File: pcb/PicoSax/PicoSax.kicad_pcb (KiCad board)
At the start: 2 copper layers, 100 x 160 mm, 80 parts, among them J3 Conn_01x02, M1 MountingHole_3.2mm_M3, M2 MountingHole_3.2mm_M3, M3 MountingHole_3.2mm_M3, M4 MountingHole_3.2mm_M3, M5 MountingHole_3.2mm_M3, M6 MountingHole_3.2mm_M3, SW8va1 Omron_B3K_L13L, SW8vb1 Omron_B3K_L13L, U1 Perfboard

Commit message: USB MIDI minor PCB tweaks
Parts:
- added M5: MountingHole_3.2mm_M3, MountingHole:MountingHole_3.2mm_M3, F.Cu at (125.0, 70.0)
- added M5: MountingHole_3.2mm_M3, MountingHole:MountingHole_3.2mm_M3, F.Cu at (75.0, 70.0)
- moved M6 5.00 mm to (140.0, 180.0)
- moved R16 1.00 mm to (137.0, 187.0)
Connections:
- U1 pad : (no net) -> GND
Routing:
- net /Dup: track 134.0 -> 136.9 mm
- net /Bb: track 147.4 -> 150.3 mm
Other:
- outline, holes or cut-outs redrawn

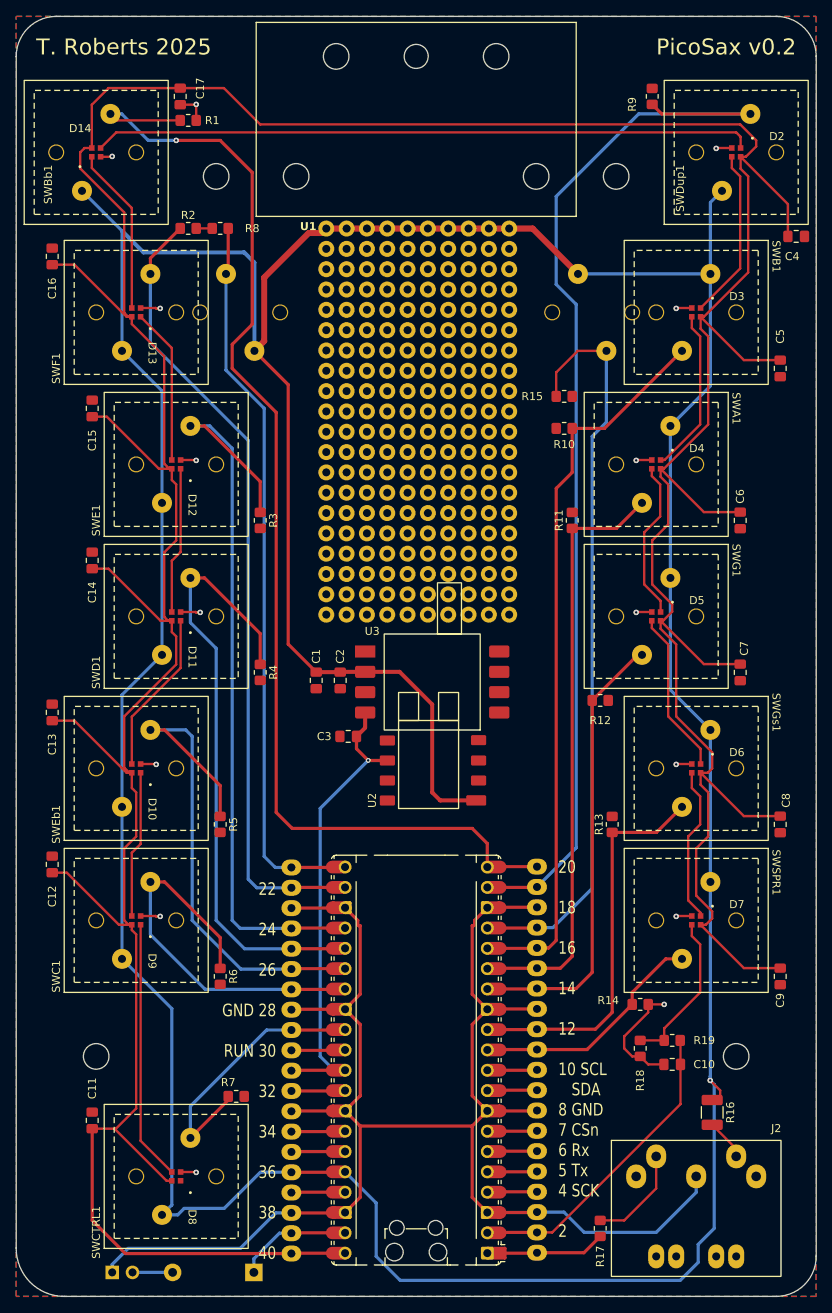
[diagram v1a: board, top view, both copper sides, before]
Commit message: KS-33 Update
Routing still required.  If wanting to work on previous version, see Backup.
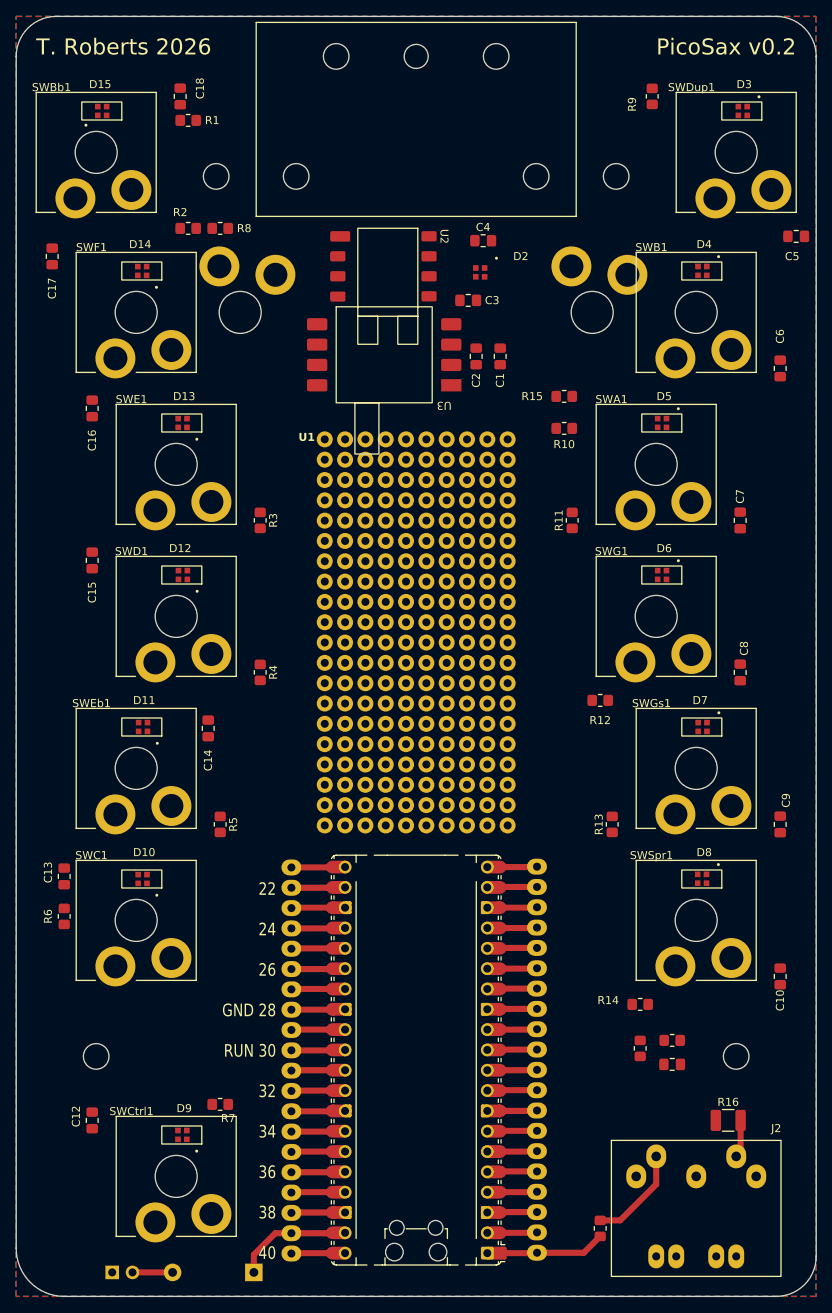
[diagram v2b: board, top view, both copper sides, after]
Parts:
- removed SWCTRL1, SWSPR1: Omron_B3K_L13L, MyLibrary:Omron B3K L13L
- added C4: 0.1uF, Capacitor_SMD:C_0805_2012Metric_Pad1.18x1.45mm_HandSolder, F.Cu at (108.4, 78.0)
- added D2: 19-C47/RSGHBHC-5V01/2T, PicoSax:19-C47_RSGHBHC-5V01-2T, F.Cu at (108.0, 82.0)
- added SWCtrl1: Gateron_KS-33, PicoSax:KS-33, F.Cu at (70.0, 195.0)
- added SWSpr1: Gateron_KS-33, PicoSax:KS-33, F.Cu at (135.0, 163.0)
- SW8va1, SW8vb1, SWA1, SWB1, SWBb1, SWC1, SWD1, SWDup1, SWE1, SWEb1, SWF1, SWG1, SWGs1: value Omron_B3K_L13L -> Gateron_KS-33; footprint MyLibrary:Omron B3K L13L -> PicoSax:KS-33
- moved U2 63.0 mm to (90.2, 82.5), turned to -90 degrees
- moved C3 56.5 mm to (106.5, 85.5), turned to 0 degrees
- moved C1 46.6 mm to (110.5, 92.5), turned to -90 degrees
- moved C2 43.9 mm to (107.5, 92.5), turned to -90 degrees
- moved U3 35.0 mm to (104.4, 96.1), turned to 0 degrees
- moved U1 26.4 mm to (88.6, 102.9)
- moved R6 20.9 mm to (56.0, 162.5), turned to 90 degrees
- moved C14 19.6 mm to (74.0, 139.0)
- moved D8 5.25 mm to (135.7, 157.8)
- moved D9 5.25 mm to (70.8, 189.8)
- moved D4 5.25 mm to (135.8, 81.8)
- moved D10 5.24 mm to (65.8, 157.8)
- moved D13 5.24 mm to (70.8, 100.8)
- moved D11 5.24 mm to (65.9, 138.8)
- moved D12 5.24 mm to (70.8, 119.8)
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- renumbered C9 to C10, C10 to C11, C11 to C12, C12 to C13, C13 to C14, C14 to C15, C15 to C16, C16 to C17, C17 to C18, C4 to C5, C5 to C6, C6 to C7, C7 to C8, C8 to C9, D9 to D10, D10 to D11, D11 to D12, D12 to D13, D13 to D14, D14 to D15, D2 to D3, D3 to D4, D4 to D5, D5 to D6, D6 to D7, D7 to D8, D8 to D9
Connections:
- A1 pad 39: Net-(A1-VSYS) -> /VSYS
- C10 pad 1: +5V -> /VSYS
- C12 pad 1: +5V -> /VSYS
- C13 pad 1: +5V -> /VSYS
- C14 pad 1: +5V -> /VSYS
- C15 pad 1: +5V -> /VSYS
- C16 pad 1: +5V -> /VSYS
- C17 pad 1: +5V -> /VSYS
- C18 pad 1: +5V -> /VSYS
- C5 pad 1: +5V -> /VSYS
- C6 pad 1: +5V -> /VSYS
- C7 pad 1: +5V -> /VSYS
- C8 pad 1: +5V -> /VSYS
- C9 pad 1: +5V -> /VSYS
- D1 pad 1: Net-(A1-VSYS) -> /VSYS
- D10 pad 2: +5V -> /VSYS
- D11 pad 2: +5V -> /VSYS
- D12 pad 2: +5V -> /VSYS
- D13 pad 2: +5V -> /VSYS
- D14 pad 2: +5V -> /VSYS
- D15 pad 2: +5V -> /VSYS
- D15 pad 3: Net-(D14-DIn) (its old number) -> Net-(D15-DIn)
- D3 pad 1: Net-(D14-DIn) (its old number) -> Net-(D2-DIn)
- D3 pad 2: +5V -> /VSYS
- D4 pad 2: +5V -> /VSYS
- D5 pad 2: +5V -> /VSYS
- D6 pad 2: +5V -> /VSYS
- D7 pad 2: +5V -> /VSYS
- D8 pad 2: +5V -> /VSYS
- D9 pad 2: +5V -> /VSYS
- J4 pad 19: Net-(A1-VSYS) -> /VSYS
- U1 pad : GND -> (no net)
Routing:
- net +5V: track 538.0 -> 6.73 mm
- net +3V3: track 534.8 -> 6.73 mm, vias 1 -> 0
- net GND: track 250.0 -> 51.8 mm, vias 15 -> 0
- net /Bb: track 150.3 -> 6.23 mm, vias 1 -> 0
- net /Dup: track 136.9 -> 6.23 mm
- net /F: track 100.5 -> 6.73 mm
- net /E: track 95.4 -> 6.73 mm
- net /8va: track 93.5 -> 6.23 mm
- net /B: track 91.6 -> 6.23 mm
- net /8vb: track 91.3 -> 6.73 mm
- net Net-(D14-DIn) (its old number): track 82.4 -> 0.00 mm
- net /D: track 77.2 -> 6.73 mm
- net /A: track 74.8 -> 6.23 mm
- net /Eb: track 65.7 -> 6.73 mm
- net Net-(A1-GPIO26_ADC0): track 59.6 -> 6.73 mm, vias 1 -> 0
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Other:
- board text added: "T. Roberts 2026"
- board text removed: "20 18 16 14 12 10 SCL SDA 8 GND 7 CSn 6 Rx 5 Tx 4 SCK 2"
- board text removed: "T. Roberts 2025"

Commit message: Partial Route
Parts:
- added R20: 0, Resistor_SMD:R_0805_2012Metric_Pad1.20x1.40mm_HandSolder, F.Cu at (57.5, 194.0)
- added R21: 0, Resistor_SMD:R_0805_2012Metric_Pad1.20x1.40mm_HandSolder, F.Cu at (57.5, 198.0)
- added R22: 0, Resistor_SMD:R_0805_2012Metric_Pad1.20x1.40mm_HandSolder, F.Cu at (57.5, 190.0)
- D1, J3: moved to F.Cu
- moved R10 27.0 mm to (144.0, 92.5), turned to 90 degrees
- moved C5 23.0 mm to (131.0, 61.5), turned to -90 degrees
- moved R2 22.3 mm to (56.0, 92.5), turned to 90 degrees
- moved R15 20.9 mm to (126.0, 78.0), turned to 180 degrees
- moved R11 19.6 mm to (139.0, 111.5)
- moved R13 19.6 mm to (144.0, 149.5)
- moved R3 19.6 mm to (61.0, 111.5), turned to 90 degrees
- moved R4 19.6 mm to (61.0, 130.5), turned to 90 degrees
- moved R5 19.6 mm to (56.0, 149.5), turned to 90 degrees
- moved C14 19.0 mm to (56.0, 145.0), turned to -90 degrees
- moved R12 16.8 mm to (139.0, 130.5), turned to 90 degrees
- moved R14 16.8 mm to (144.0, 168.5), turned to 90 degrees
- moved R9 12.6 mm to (131.0, 72.5)
- moved R1 9.82 mm to (69.0, 72.5), turned to 90 degrees
- moved C15 8.14 mm to (61.0, 126.0), turned to -90 degrees
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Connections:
- C10 pad 1: /VSYS -> /VLED
- C12 pad 1: /VSYS -> /VLED
- C13 pad 1: /VSYS -> /VLED
- C14 pad 1: /VSYS -> /VLED
- C15 pad 1: /VSYS -> /VLED
- C16 pad 1: /VSYS -> /VLED
- C17 pad 1: /VSYS -> /VLED
- C18 pad 1: /VSYS -> /VLED
- C4 pad 1: /VSYS -> /VLED
- C5 pad 1: /VSYS -> /VLED
- C6 pad 1: /VSYS -> /VLED
- C7 pad 1: /VSYS -> /VLED
- C8 pad 1: /VSYS -> /VLED
- C9 pad 1: /VSYS -> /VLED
- D10 pad 2: /VSYS -> /VLED
- D11 pad 2: /VSYS -> /VLED
- D12 pad 2: /VSYS -> /VLED
- D13 pad 2: /VSYS -> /VLED
- D14 pad 2: /VSYS -> /VLED
- D15 pad 2: /VSYS -> /VLED
- D2 pad 2: /VSYS -> /VLED
- D3 pad 2: /VSYS -> /VLED
- D4 pad 2: /VSYS -> /VLED
- D5 pad 2: /VSYS -> /VLED
- D6 pad 2: /VSYS -> /VLED
- D7 pad 2: /VSYS -> /VLED
- D8 pad 2: /VSYS -> /VLED
- D9 pad 2: /VSYS -> /VLED
- SWC1 pad 1: +3V3 -> /C
- SWC1 pad 2: /C -> +3V3
- SWD1 pad 1: +3V3 -> /D
- SWD1 pad 2: /D -> +3V3
- SWDup1 pad 1: +3V3 -> /Dup
- SWDup1 pad 2: /Dup -> +3V3
- SWE1 pad 1: +3V3 -> /E
- SWE1 pad 2: /E -> +3V3
- SWEb1 pad 1: +3V3 -> /Eb
- SWEb1 pad 2: /Eb -> +3V3
- SWF1 pad 1: +3V3 -> /F
- SWF1 pad 2: /F -> +3V3
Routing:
- net /VLED: track 0.00 -> 522.2 mm
- net +3V3: track 6.73 -> 424.1 mm, vias 0 -> 2
- net /Bb: track 6.23 -> 132.2 mm, vias 0 -> 1
- net Net-(A1-GPIO26_ADC0): track 6.73 -> 122.3 mm, vias 0 -> 1
- net /Dup: track 6.23 -> 110.2 mm
- net GND: track 51.8 -> 146.3 mm
- net /B: track 6.23 -> 99.9 mm, vias 0 -> 1
- net /8va: track 6.23 -> 97.9 mm
- net /A: track 6.23 -> 79.6 mm, vias 0 -> 1
- net /G: track 6.23 -> 63.1 mm, vias 0 -> 1
- net Net-(D15-DIn): track 0.00 -> 54.3 mm
- net /Gs: track 6.23 -> 50.9 mm, vias 0 -> 1
- net Net-(D2-DIn): track 0.00 -> 44.4 mm
- net +5V: track 6.73 -> 51.1 mm
- net /Spr: track 6.23 -> 40.6 mm
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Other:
- board text added: "19 17 15 13 11 9 7 5 3 1"
- board text added: "4.5-5.5V"
- board text removed: "1.8-5.5V"

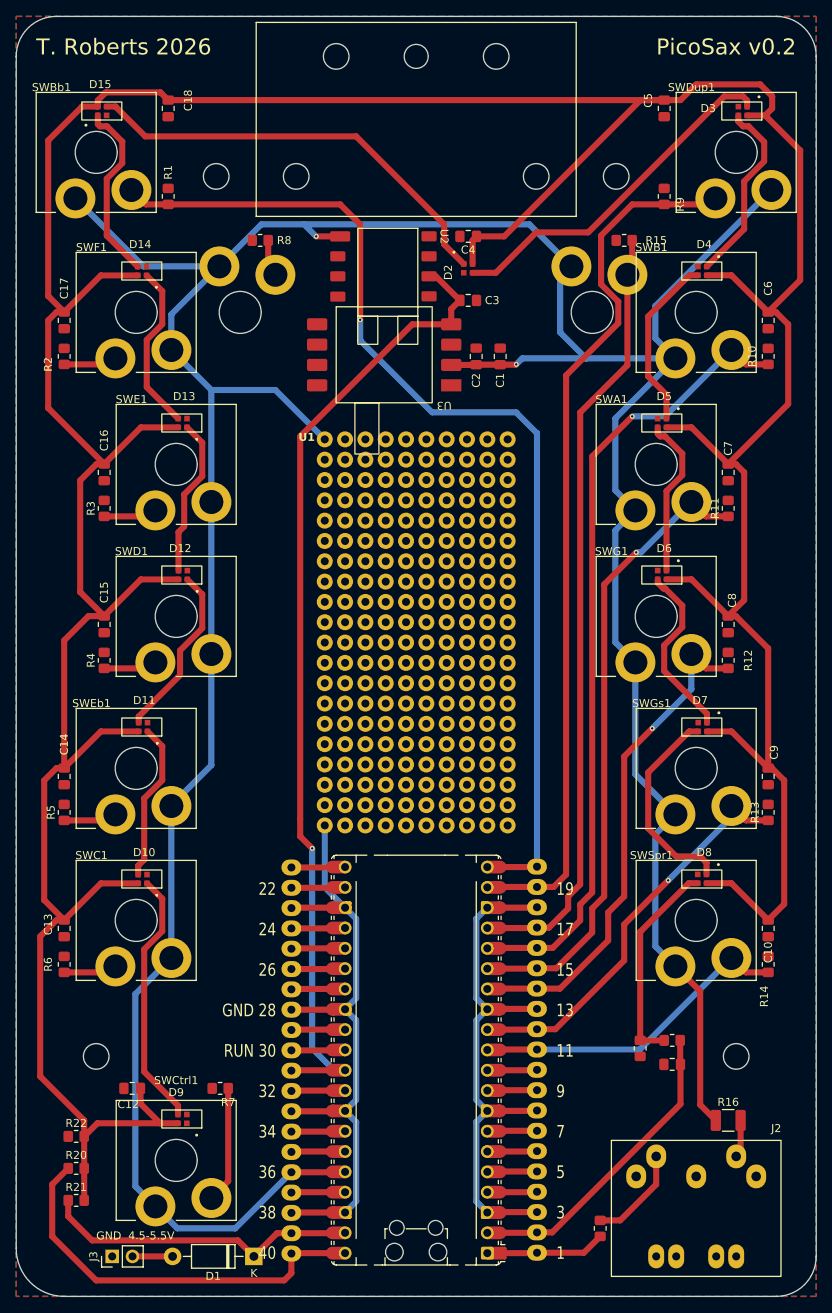
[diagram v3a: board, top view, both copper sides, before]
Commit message: Routing Complete
Still need to adjust locations of component references.  And there is an issue in DRC about the footprints not matching.  Not sure why that is as it wasn't a problem yesterday.
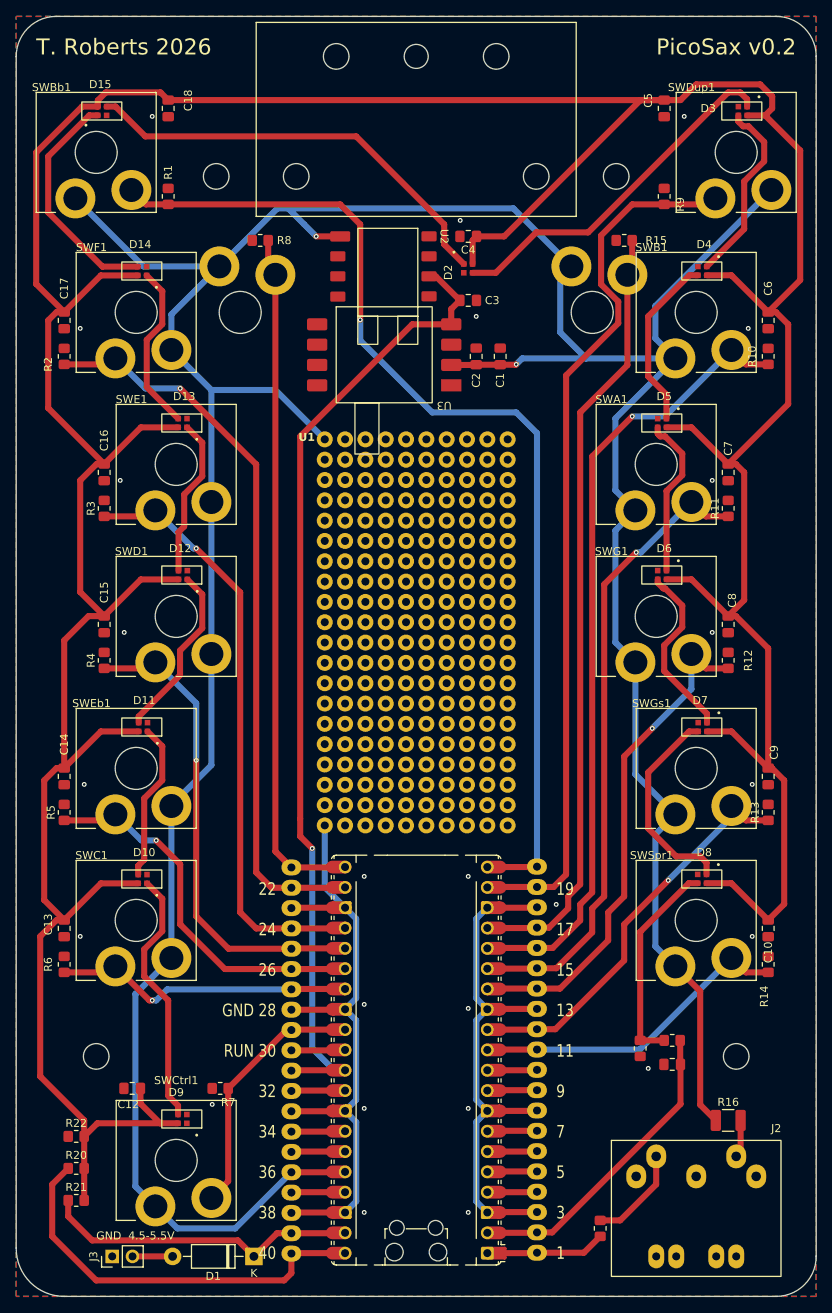
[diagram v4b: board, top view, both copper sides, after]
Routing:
- net /F: track 13.4 -> 92.7 mm, vias 0 -> 1
- net /8vb: track 11.4 -> 86.3 mm
- net /E: track 13.4 -> 75.5 mm, vias 0 -> 1
- net /D: track 13.4 -> 60.9 mm, vias 0 -> 1
- net /Eb: track 13.4 -> 47.8 mm, vias 0 -> 1
- net /C: track 13.4 -> 37.8 mm, vias 0 -> 1
- net /Ctrl: track 21.3 -> 32.2 mm
- net Net-(D14-DIn): track 23.1 -> 29.3 mm
- net +3V3: track 424.1 -> 428.6 mm
- net /VLED: track 522.2 -> 523.4 mm
- net GND: vias 0 -> 25

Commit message: V2 ready
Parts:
- added M8: MountingHole_5.5mm, MountingHole:MountingHole_5.5mm, F.Cu at (111.5, 86.5)
- moved C3 4.27 mm to (105.0, 81.5), turned to 90 degrees
- moved D2 4.03 mm to (106.0, 77.5)
- moved C4 3.54 mm to (110.0, 77.0), turned to 0 degrees
- moved C1 2.00 mm to (110.5, 94.5), turned to 90 degrees
- moved C2 2.00 mm to (107.5, 94.5), turned to 90 degrees
- renumbered M5 to M6, REF** to M7
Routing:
- net /VLED: track 523.4 -> 511.3 mm
- net Net-(D15-DIn): track 54.3 -> 50.6 mm
- net Net-(A1-GPIO26_ADC0): track 122.3 -> 123.5 mm
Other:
- board text added: "22 24 26 GND 28 RUN 30 32 34 36 38 39"
- board text added: "3.3V"
- board text added: "5V"
- board text added: "Bridge ONLY 1"
- board text added: "N/C"
- board text added: "V LED"
- board text added: "VSYS"
- board text removed: "22 24 26 GND 28 RUN 30 32 34 36 38 40"
